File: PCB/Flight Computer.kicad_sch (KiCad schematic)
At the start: 0 parts

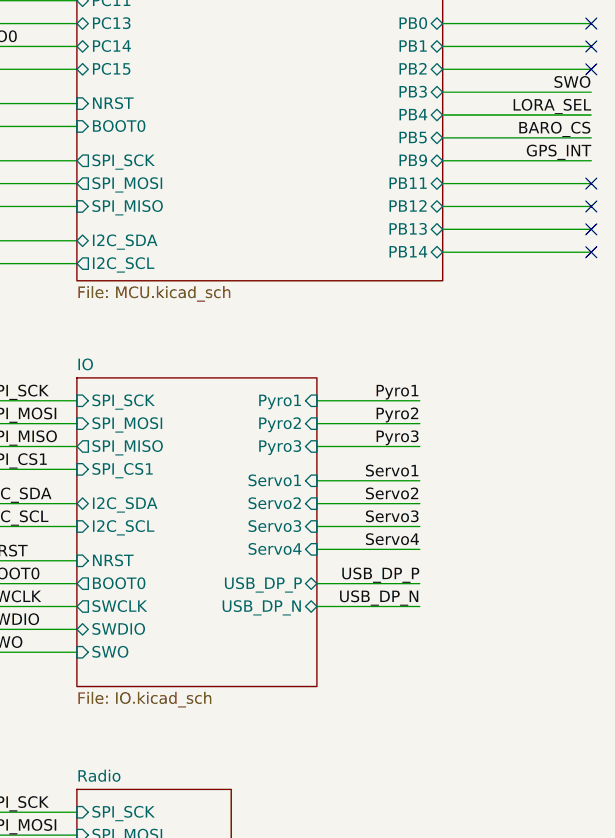
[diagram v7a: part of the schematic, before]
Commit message: Added basic buzzer, LED, and fiducials to the schematic
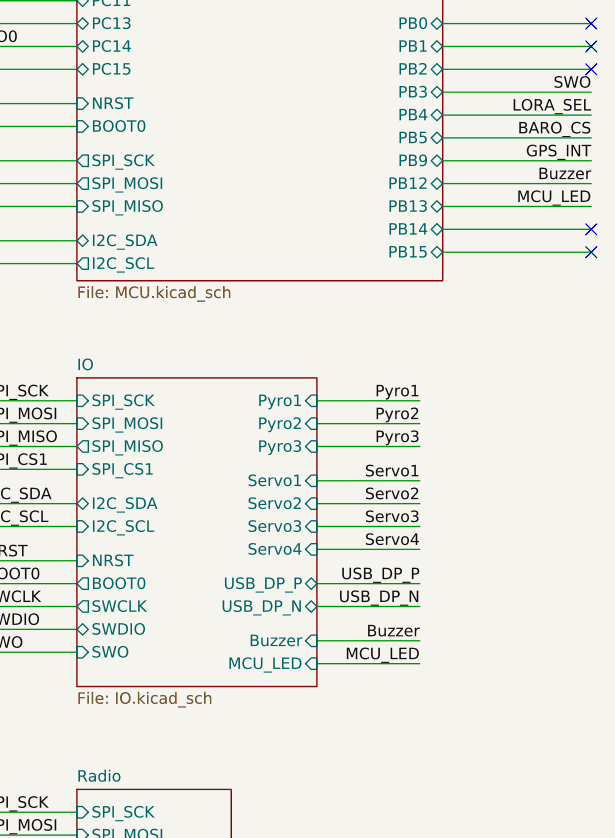
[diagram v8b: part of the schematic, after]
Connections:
- no-connect marks 19 -> 17
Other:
- sheet IO ports: added Buzzer, MCU_LED; removed none
- sheet MCU ports: added PB15; removed PB11
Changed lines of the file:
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@@
 	)
 	(no_connect
-		(at 173.99 83.82)
-	)
-	(no_connect
 		(at 100.33 45.72)
 	)
@@
 	)
 	(no_connect
-		(at 173.99 86.36)
-	)
-	(no_connect
 		(at 173.99 41.91)
 	)
@@
 	(wire
 		(pts
+			(xy 173.99 88.9) (xy 157.48 88.9)
+		)
+		(stroke
+			(width 0)
+			(type default)
+		)
+	)
+	(wire
+		(pts
 			(xy 157.48 83.82) (xy 173.99 83.82)
 		)
@@
 	(wire
 		(pts
-			(xy 157.48 91.44) (xy 173.99 91.44)
-		)
-		(stroke
-			(width 0)
-			(type default)
-		)
-	)
-	(wire
-		(pts
 			(xy 173.99 46.99) (xy 157.48 46.99)
 		)
@@
 	(wire
 		(pts
+			(xy 157.48 86.36) (xy 173.99 86.36)
+		)
+		(stroke
+			(width 0)
+			(type default)
+		)
+	)
+	(wire
+		(pts
 			(xy 100.33 53.34) (xy 116.84 53.34)
 		)
@@
 	(wire
 		(pts
+			(xy 143.51 137.16) (xy 154.94 137.16)
+		)
+		(stroke
+			(width 0)
+			(type default)
+		)
+	)
+	(wire
+		(pts
 			(xy 106.68 125.73) (xy 116.84 125.73)
 		)
@@
 	(wire
 		(pts
-			(xy 157.48 86.36) (xy 173.99 86.36)
-		)
-		(stroke
-			(width 0)
-			(type default)
-		)
-	)
-	(wire
-		(pts
 			(xy 154.94 110.49) (xy 143.51 110.49)
 		)
@@
 	(wire
 		(pts
-			(xy 157.48 88.9) (xy 173.99 88.9)
+			(xy 157.48 91.44) (xy 173.99 91.44)
+		)
+		(stroke
+			(width 0)
+			(type default)
+		)
+	)
+	(wire
+		(pts
+			(xy 143.51 134.62) (xy 154.94 134.62)
 		)
 		(stroke
@@
 		)
 	)
+	(label "MCU_LED"
+		(at 173.99 86.36 180)
+		(effects
+			(font
+				(size 1.27 1.27)
+			)
+			(justify right bottom)
+		)
+	)
 	(label "Pyro1_Cont"
 		(at 173.99 34.29 180)
@@
 		)
 	)
+	(label "Buzzer"
+		(at 154.94 134.62 180)
+		(effects
+			(font
+				(size 1.27 1.27)
+			)
+			(justify right bottom)
+		)
+	)
 	(label "GPS_RX"
 		(at 100.33 60.96 0)
@@
 		)
 	)
+	(label "Buzzer"
+		(at 173.99 83.82 180)
+		(effects
+			(font
+				(size 1.27 1.27)
+			)
+			(justify right bottom)
+		)
+	)
 	(label "Armed"
 		(at 173.99 36.83 180)
@@
 		)
 	)
+	(label "MCU_LED"
+		(at 154.94 137.16 180)
+		(effects
+			(font
+				(size 1.27 1.27)
+			)
+			(justify right bottom)
+		)
+	)
 	(label "SPI_MISO"
 		(at 88.9 86.36 180)
@@
 			)
 		)
+		(pin "Buzzer" input
+			(at 143.51 134.62 0)
+			(effects
+				(font
+					(size 1.27 1.27)
+				)
+				(justify right)
+			)
+		)
+		(pin "MCU_LED" input
+			(at 143.51 137.16 0)
+			(effects
+				(font
+					(size 1.27 1.27)
+				)
+				(justify right)
+			)
+		)
 		(instances
 			(project "Flight Computer"
@@
 			)
 		)
-		(pin "PB11" bidirectional
-			(at 157.48 83.82 0)
-			(effects
-				(font
-					(size 1.27 1.27)
-				)
-				(justify right)
-			)
-		)
 		(pin "PB13" bidirectional
-			(at 157.48 88.9 0)
+			(at 157.48 86.36 0)
 			(effects
 				(font
@@
 		)
 		(pin "PB14" bidirectional
-			(at 157.48 91.44 0)
+			(at 157.48 88.9 0)
 			(effects
 				(font
@@
 		)
 		(pin "PB12" bidirectional
-			(at 157.48 86.36 0)
+			(at 157.48 83.82 0)
 			(effects
 				(font
@@
 			(effects
 				(font
+					(size 1.27 1.27)
+				)
+				(justify right)
+			)
+		)
+		(pin "PB15" bidirectional
+			(at 157.48 91.44 0)
+			(effects
+				(font
